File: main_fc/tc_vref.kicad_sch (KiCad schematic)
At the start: 3 parts, among them U3 OP777ARZ

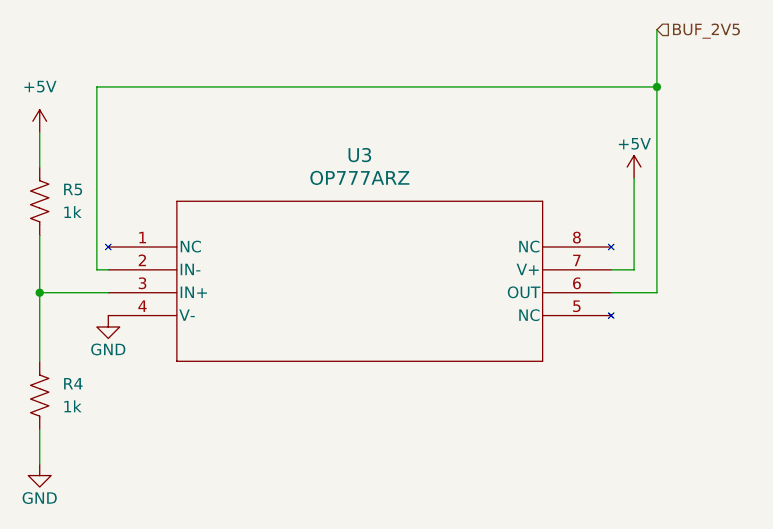
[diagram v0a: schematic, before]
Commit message: main flight computer annotations and passive footprints
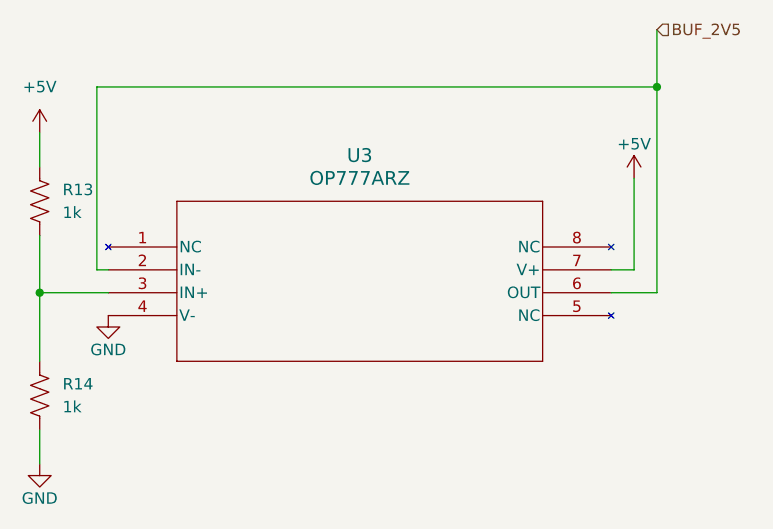
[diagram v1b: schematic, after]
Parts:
- R13: renamed from R5; footprint Resistor_SMD:R_0201_0603Metric -> Resistor_SMD:R_0603_1608Metric
- R14: renamed from R4; footprint Resistor_SMD:R_0201_0603Metric -> Resistor_SMD:R_0603_1608Metric
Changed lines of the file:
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@@
 		(dnp no)
 		(fields_autoplaced yes)
-		(property "Reference" "R5"
+		(property "Reference" "R13"
 			(at 104.14 97.7899 0)
 			(effects
@@
 			)
 		)
-		(property "Footprint" "Resistor_SMD:R_0201_0603Metric"
+		(property "Footprint" "Resistor_SMD:R_0603_1608Metric"
 			(at 102.616 99.314 90)
 			(effects
@@
 			(project "main_fc"
 				(path "/2e5bfe72-277e-40a6-babb-0928c11aa964/a49bae17-fa63-4253-a1a4-787b012d478b"
-					(reference "R5")
+					(reference "R13")
 					(unit 1)
 				)
@@
 		(dnp no)
 		(fields_autoplaced yes)
-		(property "Reference" "R4"
+		(property "Reference" "R14"
 			(at 104.14 119.3799 0)
 			(effects
@@
 			)
 		)
-		(property "Footprint" "Resistor_SMD:R_0201_0603Metric"
+		(property "Footprint" "Resistor_SMD:R_0603_1608Metric"
 			(at 102.616 120.904 90)
 			(effects
@@
 			(project "main_fc"
 				(path "/2e5bfe72-277e-40a6-babb-0928c11aa964/a49bae17-fa63-4253-a1a4-787b012d478b"
-					(reference "R4")
+					(reference "R14")
 					(unit 1)
 				)
@@
 		(on_board yes)
 		(dnp no)
-		(property "Reference" "#PWR016"
+		(property "Reference" "#PWR025"
 			(at 109.22 118.11 0)
 			(effects
@@
 			(project "main_fc"
 				(path "/2e5bfe72-277e-40a6-babb-0928c11aa964/a49bae17-fa63-4253-a1a4-787b012d478b"
-					(reference "#PWR016")
+					(reference "#PWR025")
 					(unit 1)
 				)
@@
 		(on_board yes)
 		(dnp no)
-		(property "Reference" "#PWR015"
+		(property "Reference" "#PWR026"
 			(at 167.64 100.33 0)
 			(effects
@@
 			(project "main_fc"
 				(path "/2e5bfe72-277e-40a6-babb-0928c11aa964/a49bae17-fa63-4253-a1a4-787b012d478b"
-					(reference "#PWR015")
+					(reference "#PWR026")
 					(unit 1)
 				)
@@
 		(dnp no)
 		(fields_autoplaced yes)
-		(property "Reference" "#PWR017"
+		(property "Reference" "#PWR023"
 			(at 101.6 95.25 0)
 			(effects
@@
 			(project "main_fc"
 				(path "/2e5bfe72-277e-40a6-babb-0928c11aa964/a49bae17-fa63-4253-a1a4-787b012d478b"
-					(reference "#PWR017")
+					(reference "#PWR023")
 					(unit 1)
 				)
@@
 		(on_board yes)
 		(dnp no)
-		(property "Reference" "#PWR0127"
+		(property "Reference" "#PWR024"
 			(at 101.6 134.62 0)
 			(effects
@@
 			(project "main_fc"
 				(path "/2e5bfe72-277e-40a6-babb-0928c11aa964/a49bae17-fa63-4253-a1a4-787b012d478b"
-					(reference "#PWR0127")
-					(unit 1)
-				)
+					(reference "#PWR024")
+					(unit 1)
+				)

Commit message: updated library
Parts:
- U3: footprint ul_ADS1158IRTCR:R_8_ADI -> avi_footprint:R_8_ADI-M
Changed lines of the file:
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@@
 			)
 		)
-		(property "Footprint" "ul_ADS1158IRTCR:R_8_ADI"
+		(property "Footprint" "avi_footprint:R_8_ADI-M"
 			(at 109.22 104.14 0)
 			(effects

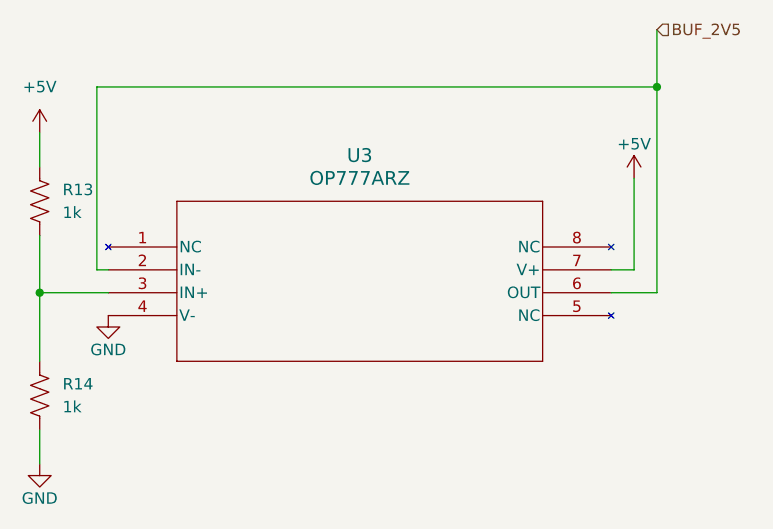
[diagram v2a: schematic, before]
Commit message: added new stm symbol/footprint
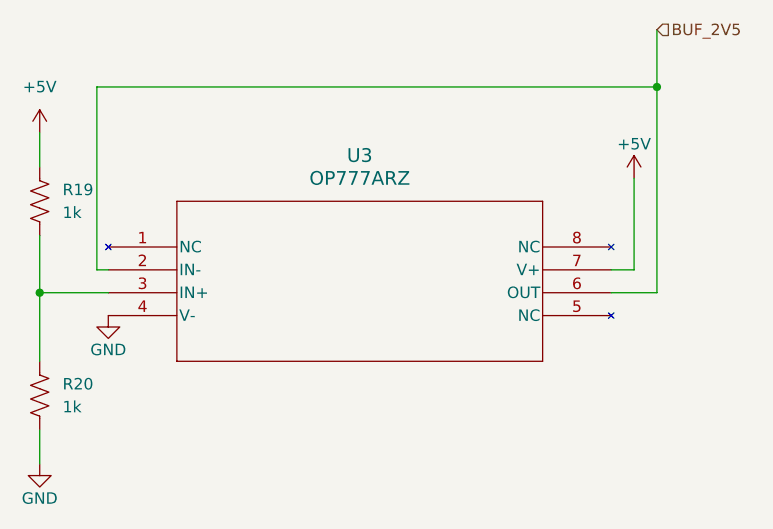
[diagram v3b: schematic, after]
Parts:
- renumbered R13 to R19, R14 to R20
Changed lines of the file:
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@@
 		(dnp no)
 		(fields_autoplaced yes)
-		(property "Reference" "R13"
+		(property "Reference" "R19"
 			(at 104.14 97.7899 0)
 			(effects
@@
 			(project "main_fc"
 				(path "/2e5bfe72-277e-40a6-babb-0928c11aa964/a49bae17-fa63-4253-a1a4-787b012d478b"
-					(reference "R13")
+					(reference "R19")
 					(unit 1)
 				)
@@
 		(dnp no)
 		(fields_autoplaced yes)
-		(property "Reference" "R14"
+		(property "Reference" "R20"
 			(at 104.14 119.3799 0)
 			(effects
@@
 			(project "main_fc"
 				(path "/2e5bfe72-277e-40a6-babb-0928c11aa964/a49bae17-fa63-4253-a1a4-787b012d478b"
-					(reference "R14")
+					(reference "R20")
 					(unit 1)
 				)
@@
 		(on_board yes)
 		(dnp no)
-		(property "Reference" "#PWR025"
+		(property "Reference" "#PWR023"
 			(at 109.22 118.11 0)
 			(effects
@@
 			(project "main_fc"
 				(path "/2e5bfe72-277e-40a6-babb-0928c11aa964/a49bae17-fa63-4253-a1a4-787b012d478b"
-					(reference "#PWR025")
+					(reference "#PWR023")
 					(unit 1)
 				)
@@
 		(on_board yes)
 		(dnp no)
-		(property "Reference" "#PWR026"
+		(property "Reference" "#PWR024"
 			(at 167.64 100.33 0)
 			(effects
@@
 			(project "main_fc"
 				(path "/2e5bfe72-277e-40a6-babb-0928c11aa964/a49bae17-fa63-4253-a1a4-787b012d478b"
-					(reference "#PWR026")
+					(reference "#PWR024")
 					(unit 1)
 				)
@@
 		(dnp no)
 		(fields_autoplaced yes)
-		(property "Reference" "#PWR023"
+		(property "Reference" "#PWR021"
 			(at 101.6 95.25 0)
 			(effects
@@
 			(project "main_fc"
 				(path "/2e5bfe72-277e-40a6-babb-0928c11aa964/a49bae17-fa63-4253-a1a4-787b012d478b"
-					(reference "#PWR023")
+					(reference "#PWR021")
 					(unit 1)
 				)
@@
 		(on_board yes)
 		(dnp no)
-		(property "Reference" "#PWR024"
+		(property "Reference" "#PWR022"
 			(at 101.6 134.62 0)
 			(effects
@@
 			(project "main_fc"
 				(path "/2e5bfe72-277e-40a6-babb-0928c11aa964/a49bae17-fa63-4253-a1a4-787b012d478b"
-					(reference "#PWR024")
-					(unit 1)
-				)
+					(reference "#PWR022")
+					(unit 1)
+				)
